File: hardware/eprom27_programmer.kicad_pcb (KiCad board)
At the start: 2 copper layers, 76.5 x 80 mm, 41 parts, among them IC1 74HC595D, IC2 74HC595D, Q1 BC557, Q2 BC557, Q3 BC557, Q4 BC557, Q5 BC557, Q6 BC547, Q7 BC547, Q8 BC547, U1 NANO, U2 DC-DC-STEP-UP-MT3608

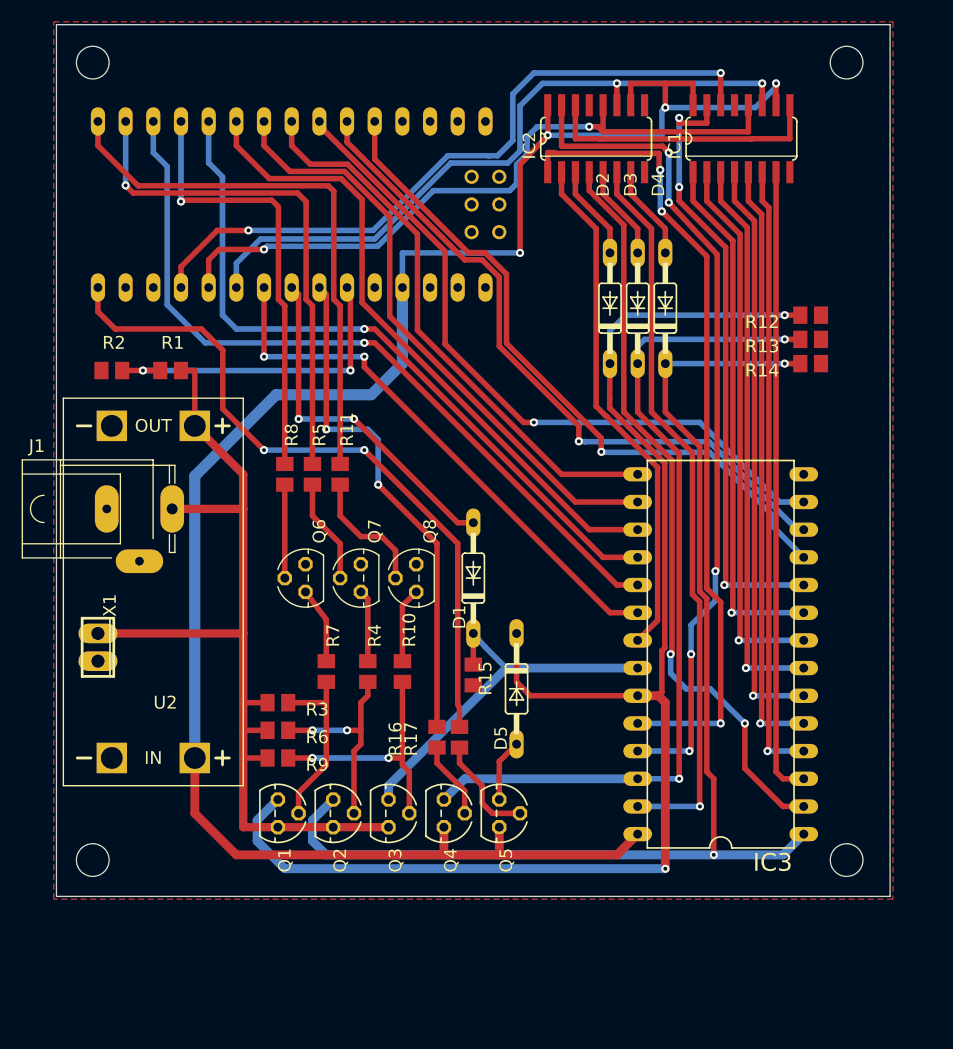
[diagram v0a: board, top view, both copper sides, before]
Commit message: Change symbols to KiCAD Symbols Change footrpints to KiCAD footprints Redesign as all through-hole components Update gitignore
Signed-off-by: Ilias Daradimos <judgedrid@gmail.com>
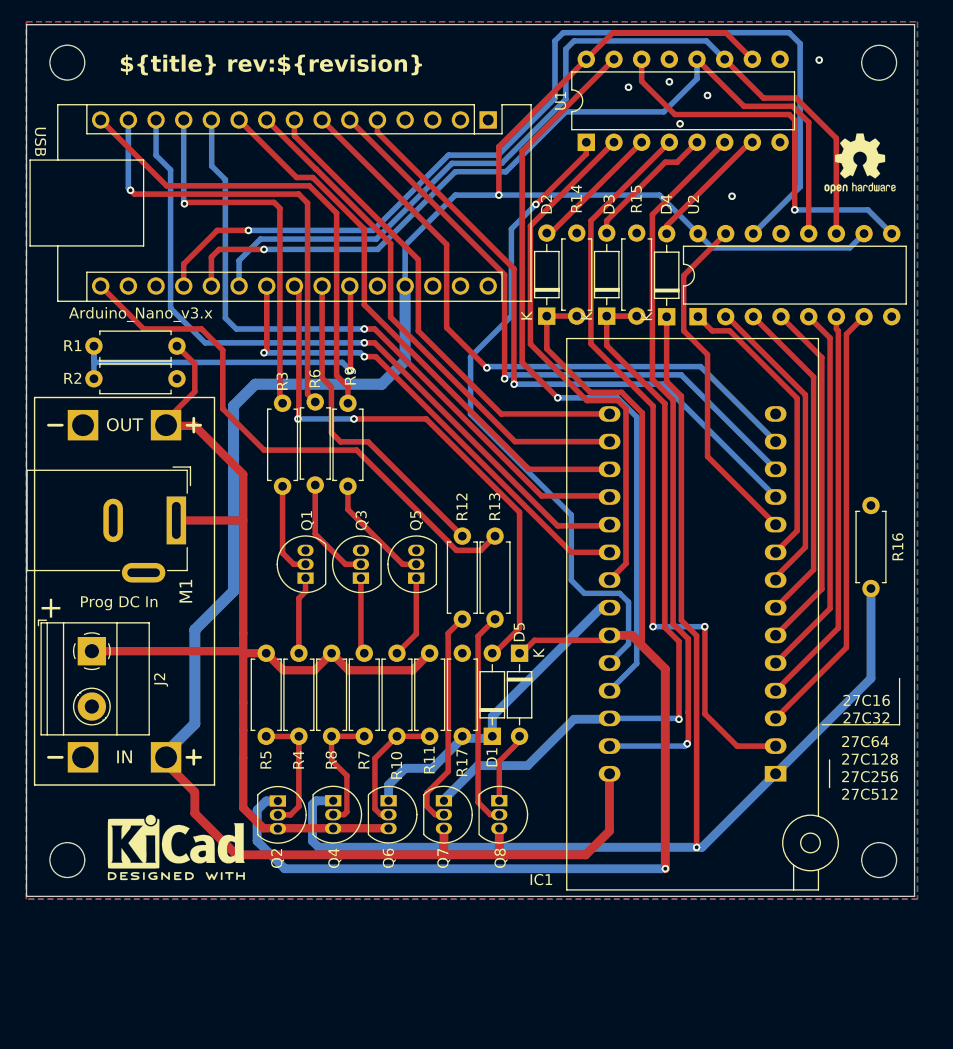
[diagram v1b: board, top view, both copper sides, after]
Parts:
- removed @HOLE0, @HOLE1, @HOLE2, @HOLE3: , 
- removed the IC1 at (173.1, 75.5)
- removed IC2: 74HC595D, untitled:SO16
- removed X1: , untitled:2POL254
- added A1: Arduino_Nano_v3.x, Module:Arduino_Nano, F.Cu at (149.9, 73.8)
- added J2: Prog DC In, TerminalBlock_Phoenix:TerminalBlock_Phoenix_MKDS-1,5-2-5.08_1x02_P5.08mm_Horizontal, F.Cu at (113.5, 122.5)
- added REF**: MountingHole_3.2mm_M3_DIN965, MountingHole:MountingHole_3.2mm_M3_DIN965, F.Cu at (111.2, 68.5)
- added REF**: MountingHole_3.2mm_M3_DIN965, MountingHole:MountingHole_3.2mm_M3_DIN965, F.Cu at (185.8, 68.5)
- added REF**: MountingHole_3.2mm_M3_DIN965, MountingHole:MountingHole_3.2mm_M3_DIN965, F.Cu at (185.8, 141.7)
- added REF**: KiCad-Logo2_5mm_SilkScreen, Symbol:KiCad-Logo2_5mm_SilkScreen, F.Cu at (121.2, 140.5)
- added REF**: MountingHole_3.2mm_M3_DIN965, MountingHole:MountingHole_3.2mm_M3_DIN965, F.Cu at (111.2, 141.7)
- added REF**: OSHW-Logo2_7.3x6mm_SilkScreen, Symbol:OSHW-Logo2_7.3x6mm_SilkScreen, F.Cu at (184.0, 77.8)
- added U2: 74HC595, Package_DIP:DIP-16_W7.62mm, F.Cu at (169.1, 91.8)
- D1, D2, D3, D4, D5: footprint untitled:DO35-10 -> Diode_THT:D_DO-35_SOD27_P7.62mm_Horizontal
- IC1: renamed from IC3; value (none) -> EPROM; footprint untitled:DIL28 -> Socket:DIP_Socket-28_W11.9_W12.7_W15.24_W17.78_W18.5_3M_228-1277-00-0602J
- J1: value (none) -> Prog DC In; footprint untitled:SPC4078 -> Connector_BarrelJack:BarrelJack_Wuerth_6941xx301002
- M1: renamed from U2; value DC-DC-STEP-UP-MT3608 -> MT3608; footprint untitled:DC-DC-STEP-UP-MT3608 -> eprom27:DC-DC-STEP-UP-MT3608
- Q1: renamed from Q6; footprint untitled:TO92 -> Package_TO_SOT_THT:TO-92_Inline
- Q2: renamed from Q1; footprint untitled:TO92 -> Package_TO_SOT_THT:TO-92_Inline
- Q3: renamed from Q7; footprint untitled:TO92 -> Package_TO_SOT_THT:TO-92_Inline
- Q4: renamed from Q2; footprint untitled:TO92 -> Package_TO_SOT_THT:TO-92_Inline
- Q5: renamed from Q8; footprint untitled:TO92 -> Package_TO_SOT_THT:TO-92_Inline
- Q6: renamed from Q3; footprint untitled:TO92 -> Package_TO_SOT_THT:TO-92_Inline
- Q7: renamed from Q4; footprint untitled:TO92 -> Package_TO_SOT_THT:TO-92_Inline
- Q8: renamed from Q5; footprint untitled:TO92 -> Package_TO_SOT_THT:TO-92_Inline
- R1: value (none) -> 10k; footprint untitled:M0805 -> Resistor_THT:R_Axial_DIN0207_L6.3mm_D2.5mm_P7.62mm_Horizontal
- R10: footprint untitled:M0805 -> Resistor_THT:R_Axial_DIN0207_L6.3mm_D2.5mm_P7.62mm_Horizontal
- R11: renamed from R9; footprint untitled:M0805 -> Resistor_THT:R_Axial_DIN0207_L6.3mm_D2.5mm_P7.62mm_Horizontal
- R12: renamed from R16; footprint untitled:M0805 -> Resistor_THT:R_Axial_DIN0207_L6.3mm_D2.5mm_P7.62mm_Horizontal
- R13: renamed from R17; footprint untitled:M0805 -> Resistor_THT:R_Axial_DIN0207_L6.3mm_D2.5mm_P7.62mm_Horizontal
- R14: renamed from R12; footprint untitled:M0805 -> Resistor_THT:R_Axial_DIN0207_L6.3mm_D2.5mm_P7.62mm_Horizontal
- R15: renamed from R13; footprint untitled:M0805 -> Resistor_THT:R_Axial_DIN0207_L6.3mm_D2.5mm_P7.62mm_Horizontal
- R16: renamed from R14; footprint untitled:M0805 -> Resistor_THT:R_Axial_DIN0207_L6.3mm_D2.5mm_P7.62mm_Horizontal
- R17: renamed from R15; footprint untitled:M0805 -> Resistor_THT:R_Axial_DIN0207_L6.3mm_D2.5mm_P7.62mm_Horizontal
- R2: value (none) -> 15k; footprint untitled:M0805 -> Resistor_THT:R_Axial_DIN0207_L6.3mm_D2.5mm_P7.62mm_Horizontal
- R3: renamed from R8; footprint untitled:M0805 -> Resistor_THT:R_Axial_DIN0207_L6.3mm_D2.5mm_P7.62mm_Horizontal
- R4: renamed from R7; footprint untitled:M0805 -> Resistor_THT:R_Axial_DIN0207_L6.3mm_D2.5mm_P7.62mm_Horizontal
- R5: renamed from R3; footprint untitled:M0805 -> Resistor_THT:R_Axial_DIN0207_L6.3mm_D2.5mm_P7.62mm_Horizontal
- R6: renamed from R5; footprint untitled:M0805 -> Resistor_THT:R_Axial_DIN0207_L6.3mm_D2.5mm_P7.62mm_Horizontal
- R7: renamed from R4; footprint untitled:M0805 -> Resistor_THT:R_Axial_DIN0207_L6.3mm_D2.5mm_P7.62mm_Horizontal
- R8: renamed from R6; footprint untitled:M0805 -> Resistor_THT:R_Axial_DIN0207_L6.3mm_D2.5mm_P7.62mm_Horizontal
- R9: renamed from R11; footprint untitled:M0805 -> Resistor_THT:R_Axial_DIN0207_L6.3mm_D2.5mm_P7.62mm_Horizontal
- U1: value NANO -> 74HC595; footprint untitled:NANO -> Package_DIP:DIP-16_W7.62mm
- moved R14 21.5 mm to (158.0, 91.8), turned to 90 degrees
- moved R16 21.4 mm to (185.0, 116.8), turned to 90 degrees
- moved R13 18.7 mm to (150.5, 111.9)
- moved R12 18.6 mm to (147.5, 111.9)
- moved U1 18.4 mm to (158.9, 75.8)
- moved R15 16.1 mm to (163.5, 91.8), turned to 90 degrees
- moved D1 14.6 mm to (150.2, 130.3)
- moved R11 14.1 mm to (144.5, 130.3), turned to 90 degrees
- moved IC1 12.1 mm to (176.2, 133.8), turned to 180 degrees
- moved R9 6.56 mm to (137.0, 99.8)
- moved R3 6.52 mm to (131.0, 99.8)
- moved R4 6.45 mm to (132.5, 130.3)
- moved R10 5.96 mm to (141.5, 130.3)
- moved D2 5.84 mm to (155.2, 91.8)
- moved R17 5.72 mm to (147.5, 130.3), turned to 90 degrees
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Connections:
- IC1 pad 1: A15 -> /A15
- IC1 pad 10: A0 -> /A0
- IC1 pad 11: D0 -> /D0
- IC1 pad 12: D1 -> /D1
- IC1 pad 13: D2 -> /D2
- IC1 pad 15: D3 -> /D3
- IC1 pad 16: D4 -> /D4
- IC1 pad 17: D5 -> /D5
- IC1 pad 18: D6 -> /D6
- IC1 pad 19: D7 -> /D7
- IC1 pad 2: A12 -> /A12
- IC1 pad 20: CE -> /CE
- IC1 pad 21: A10 -> /A10
- IC1 pad 22: OE -> /OE
- IC1 pad 23: A11 -> /A11
- IC1 pad 24: A9 -> /A9
- IC1 pad 25: A8 -> /A8
- IC1 pad 26: A13 -> /A13
- IC1 pad 27: A14 -> /A14
- IC1 pad 3: A7 -> /A7
- IC1 pad 4: A6 -> /A6
- IC1 pad 5: A5 -> /A5
- IC1 pad 6: A4 -> /A4
- IC1 pad 7: A3 -> /A3
- IC1 pad 8: A2 -> /A2
- IC1 pad 9: A1 -> /A1
- J1 pad 1: GND -> +24V
- J1 pad 3: +24V -> GND
- Q1 pad 1: GND -> Net-(Q1-C)
- Q1 pad 3: N$22 -> GND
- Q2 pad 1: +24V -> /A11
- Q2 pad 3: A11 -> +24V
- Q3 pad 1: GND -> Net-(Q3-C)
- Q3 pad 3: N$19 -> GND
- Q4 pad 1: +24V -> /A15
- Q4 pad 3: A15 -> +24V
- Q5 pad 1: GND -> Net-(Q5-C)
- Q5 pad 3: N$16 -> GND
- Q6 pad 1: +24V -> /OE
- Q6 pad 3: OE -> +24V
- Q7 pad 1: VCC -> /A13
- Q7 pad 3: A13 -> VCC
- Q8 pad 1: VCC -> Net-(D5-A)
- Q8 pad 3: N$15 -> VCC
- R1 pad 2: N$9 -> /A_A6
- R10 pad 2: N$16 -> Net-(Q5-C)
- R12 pad 1: N$10 -> /A_A5
- R13 pad 1: N$12 -> Net-(A1-D13)
- R14 pad 1: A11 -> /A11
- R15 pad 1: A13 -> /A13
- R16 pad 1: A15 -> /A15
- R17 pad 1: OE -> /OE
- R2 pad 1: N$9 -> /A_A6
- R3 pad 1: N$7 -> Net-(A1-D9)
- R4 pad 2: N$22 -> Net-(Q1-C)
- R6 pad 2: N$11 -> Net-(A1-D11)
- R7 pad 1: N$19 -> Net-(Q3-C)
- R9 pad 1: N$13 -> Net-(A1-D12)
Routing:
- net A11: track 131.1 -> 0.00 mm, vias 2 -> 0
- net /A15: track 0.00 -> 121.4 mm, vias 0 -> 1
- net /A11: track 0.00 -> 117.4 mm, vias 0 -> 1
- net A15: track 110.3 -> 0.00 mm, vias 2 -> 0
- net /A_A0: track 0.00 -> 90.1 mm, vias 0 -> 1
- net /A_A2: track 0.00 -> 80.6 mm
- net A13: track 78.8 -> 0.00 mm, vias 2 -> 0
- net /A_A1: track 0.00 -> 78.6 mm, vias 0 -> 1
- net A8: track 76.3 -> 0.00 mm, vias 5 -> 0
- net A9: track 74.5 -> 0.00 mm, vias 3 -> 0
- net D7: track 71.2 -> 0.00 mm, vias 1 -> 0
- net /A12: track 0.00 -> 70.3 mm, vias 0 -> 2
- net /A8: track 0.00 -> 70.0 mm, vias 0 -> 1
- net A12: track 68.9 -> 0.00 mm, vias 2 -> 0
- net /A13: track 0.00 -> 67.3 mm, vias 0 -> 1
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- added copper zone on B.Cu, net GND
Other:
- board size 76.5 x 80 mm -> 81.5 x 80 mm
- board text added: "${title} rev:${revision}"
- board text added: "+"
- board text added: "27C16 27C32"
- board text added: "27C64 27C128 27C256 27C512"

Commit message: Set ADC range to 30V
Signed-off-by: Ilias Daradimos <judgedrid@gmail.com>
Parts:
- R1: value 10k -> 22k
- R2: value 15k -> 4.7k
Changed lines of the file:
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@@
         (effects (font (size 1 1) (thickness 0.15)))
     )
-    (fp_text value "15k" (at 3.81 2.37) (layer "F.Fab")
+    (fp_text value "4.7k" (at 3.81 2.37) (layer "F.Fab")
         (effects (font (size 1 1) (thickness 0.15)))
     )
@@
         (effects (font (size 1 1) (thickness 0.15)))
     )
-    (fp_text value "10k" (at 3.81 2.37 180) (layer "F.Fab")
+    (fp_text value "22k" (at 3.81 2.37 180) (layer "F.Fab")
         (effects (font (size 1 1) (thickness 0.15)))
     )
@@
     (property "ki_description" "Arduino Nano v3.x")
     (property "ki_keywords" "Arduino nano microcontroller module USB")
-    (clearance 0.1)
     (attr through_hole)
     (fp_text reference "A1" (at -2.75 -0.13 90) (layer "F.SilkS") hide
@@
     (pad "30" thru_hole oval (at 15.24 0 270) (size 1.6 1.6) (drill 1) (layers "*.Cu" "*.Mask")
       (net 59 "unconnected-(A1-VIN-Pad30)") (pinfunction "VIN") (pintype "power_in+no_connect"))
-    (model "${KICAD6_3DMODEL_DIR}/Module.3dshapes/Arduino_Nano_WithMountingHoles.wrl" hide
+    (model "${KICAD6_3DMODEL_DIR}/Module.3dshapes/Arduino_Nano_WithMountingHoles.wrl"
       (offset (xyz 0 0 0))
       (scale (xyz 1 1 1))
       (rotate (xyz 0 0 0))
-    )
-    (model ":KICAD7_3DMODEL_DIR:Connector_PinSocket_2.54mm.3dshapes/PinSocket_1x15_P2.54mm_Vertical.wrl"
-      (offset (xyz 0 0 0))
-      (scale (xyz 1 1 1))
-      (rotate (xyz 0 0 0))
-    )
-    (model ":KICAD7_3DMODEL_DIR:Connector_PinSocket_2.54mm.3dshapes/PinSocket_1x15_P2.54mm_Vertical.wrl"
-      (offset (xyz 15 0 0))
-      (scale (xyz 1 1 1))
-      (rotate (xyz 0 0 0))

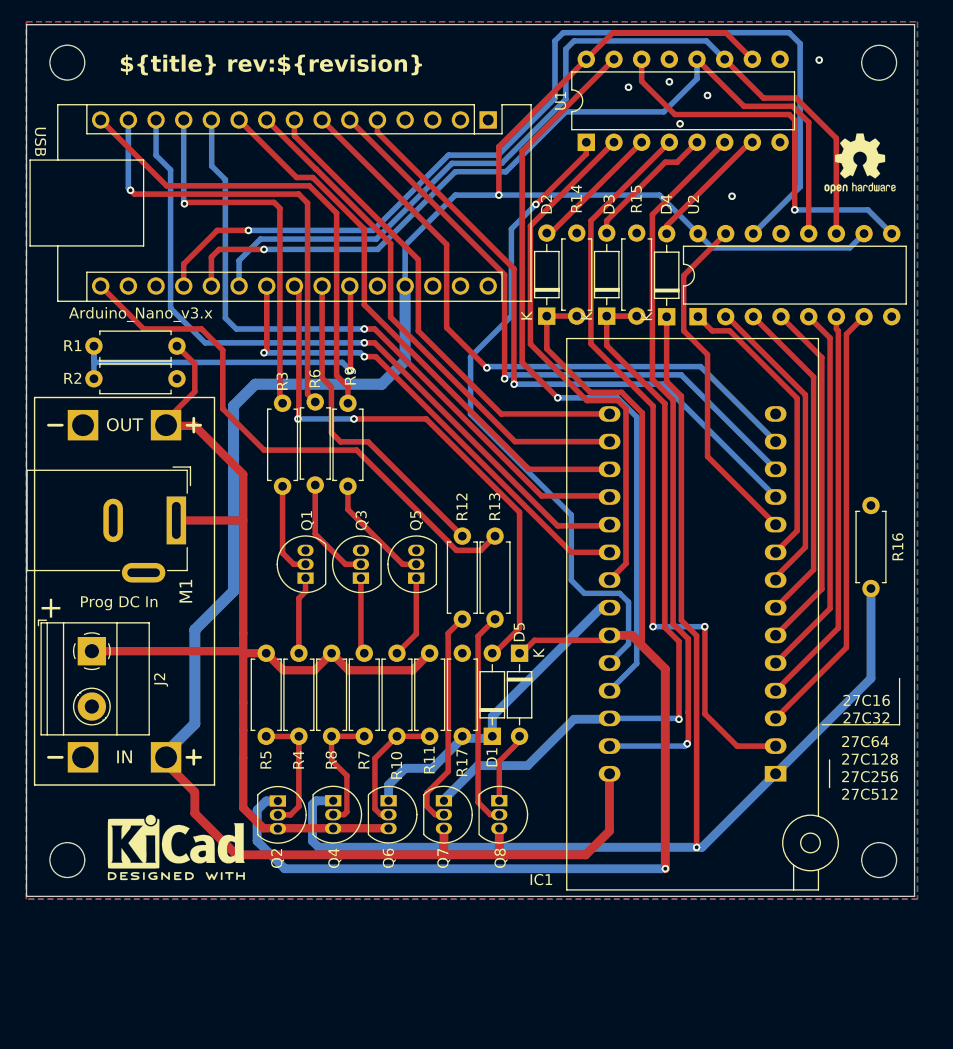
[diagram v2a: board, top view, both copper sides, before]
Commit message: Add EPROM ID and EEPROM Erase connection
Signed-off-by: Ilias Daradimos <judgedrid@gmail.com>
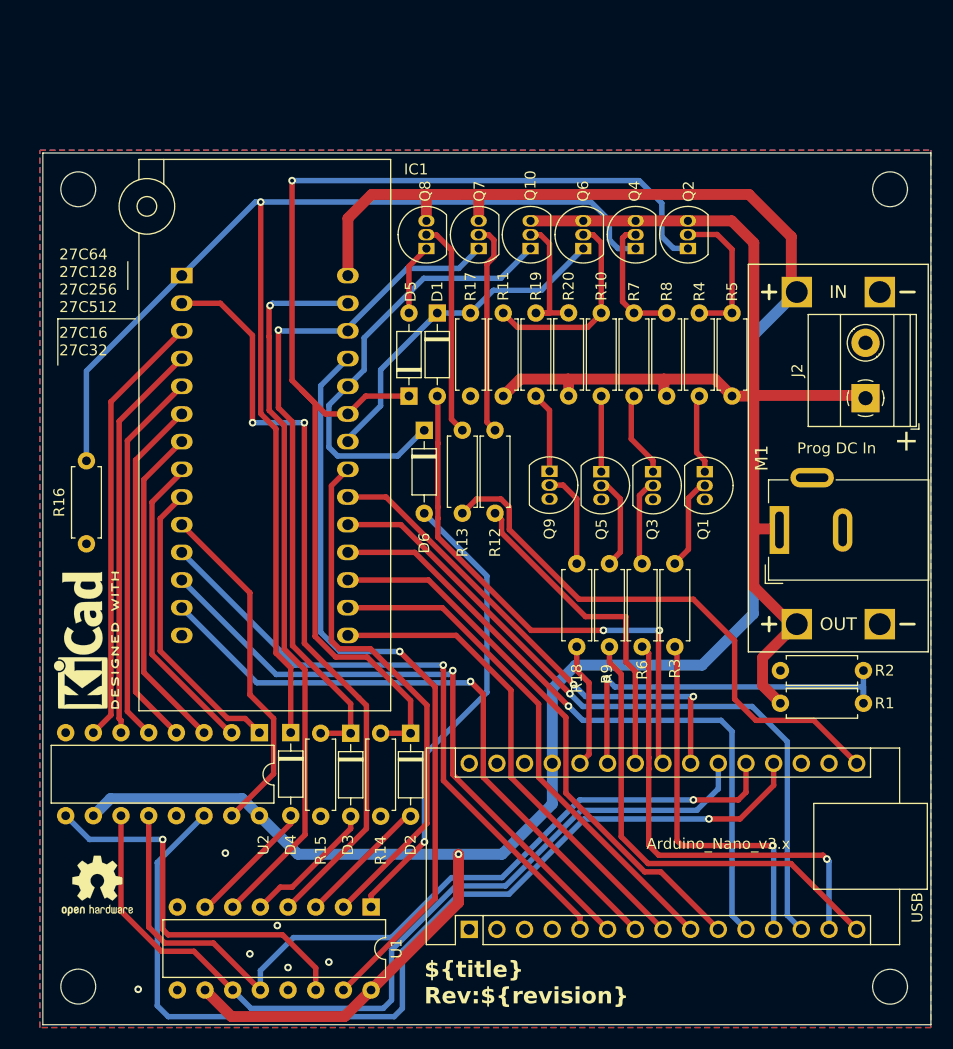
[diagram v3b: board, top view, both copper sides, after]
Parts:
- added D6: 1N4446, Diode_THT:D_DO-35_SOD27_P7.62mm_Horizontal, F.Cu at (144.0, 102.2)
- added Q10: BC557, Package_TO_SOT_THT:TO-92_Inline, F.Cu at (153.8, 85.5)
- added Q9: BC547, Package_TO_SOT_THT:TO-92_Inline, F.Cu at (155.5, 106.0)
- added R18: 22K, Resistor_THT:R_Axial_DIN0207_L6.3mm_D2.5mm_P7.62mm_Horizontal, F.Cu at (158.0, 122.1)
- added R19: 22K, Resistor_THT:R_Axial_DIN0207_L6.3mm_D2.5mm_P7.62mm_Horizontal, F.Cu at (154.2, 91.5)
- added R20: 22K, Resistor_THT:R_Axial_DIN0207_L6.3mm_D2.5mm_P7.62mm_Horizontal, F.Cu at (157.2, 91.5)
- R1: value 22k -> 10k
- moved REF** 113.5 mm to (186.8, 153.3), turned to 180 degrees
- moved REF** 112.2 mm to (112.2, 153.3), turned to 180 degrees
- moved REF** 97.4 mm to (186.8, 80.1), turned to 180 degrees
- moved REF** 96.4 mm to (114.0, 144.0)
- moved REF** 95.9 mm to (112.2, 80.1), turned to 180 degrees
- moved R2 75.5 mm to (184.3, 124.3), turned to 180 degrees
- moved J2 74.7 mm to (184.5, 99.3), turned to 90 degrees
- moved A1 74.3 mm to (148.1, 148.0), turned to 90 degrees
- moved R16 72.9 mm to (113.0, 105.0), turned to -90 degrees
- moved U1 72.9 mm to (139.1, 146.0), turned to -90 degrees
- moved IC1 71.1 mm to (121.8, 88.0), turned to 0 degrees
- moved M1 66.6 mm to (182.0, 104.8), turned to 90 degrees
- moved R1 64.4 mm to (176.7, 127.3), turned to 0 degrees
- moved Q2 63.1 mm to (168.2, 85.5), turned to 90 degrees
- moved Q4 57.8 mm to (163.4, 85.5), turned to 90 degrees
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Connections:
- A1 pad 26: unconnected-(A1-A7-Pad26) -> Net-(A1-A7)
- U1 pad 1: /A9 -> Net-(D6-A)
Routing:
- net Net-(D6-A): track 0.00 -> 42.9 mm, vias 0 -> 1
- net /A9: track 60.8 -> 40.1 mm, vias 1 -> 0
- net Net-(Q10-B): track 0.00 -> 12.7 mm
- net Net-(A1-A7): track 0.00 -> 11.5 mm
- net Net-(Q9-B): track 0.00 -> 8.98 mm
- net VCC: track 199.6 -> 207.6 mm
- net Net-(Q9-C): track 0.00 -> 7.36 mm
- net Net-(Q6-B): track 12.0 -> 18.5 mm
- net /A11: track 117.4 -> 111.8 mm
- net +24V: track 102.6 -> 107.8 mm
- net /A15: track 121.4 -> 117.7 mm
- net /A13: track 67.3 -> 64.2 mm
- net Net-(Q5-B): track 10.5 -> 8.55 mm
- net Net-(Q3-B): track 9.84 -> 8.05 mm
- net Net-(Q2-B): track 11.7 -> 13.5 mm
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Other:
- board text added: "${title} Rev:${revision}"
- board text removed: "${title} rev:${revision}"

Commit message: Change voltage naming Update voltage divider Update README
Signed-off-by: Ilias Daradimos <judgedrid@gmail.com>
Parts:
- R1: value 10k -> 33k
- R2: value 4.7k -> 6.8k
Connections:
- net +24V renamed VPP
- net VCC renamed +5V
